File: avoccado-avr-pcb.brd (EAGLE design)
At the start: 17.8 x 40.3 mm, 31 parts, among them IC1 MCP1703CB, Q1 #MHz, Q2 MOSFET-NCHANNEL2N7002PW, U1 ATMEGA168#, U2 MCP73831, X1 Micro USB

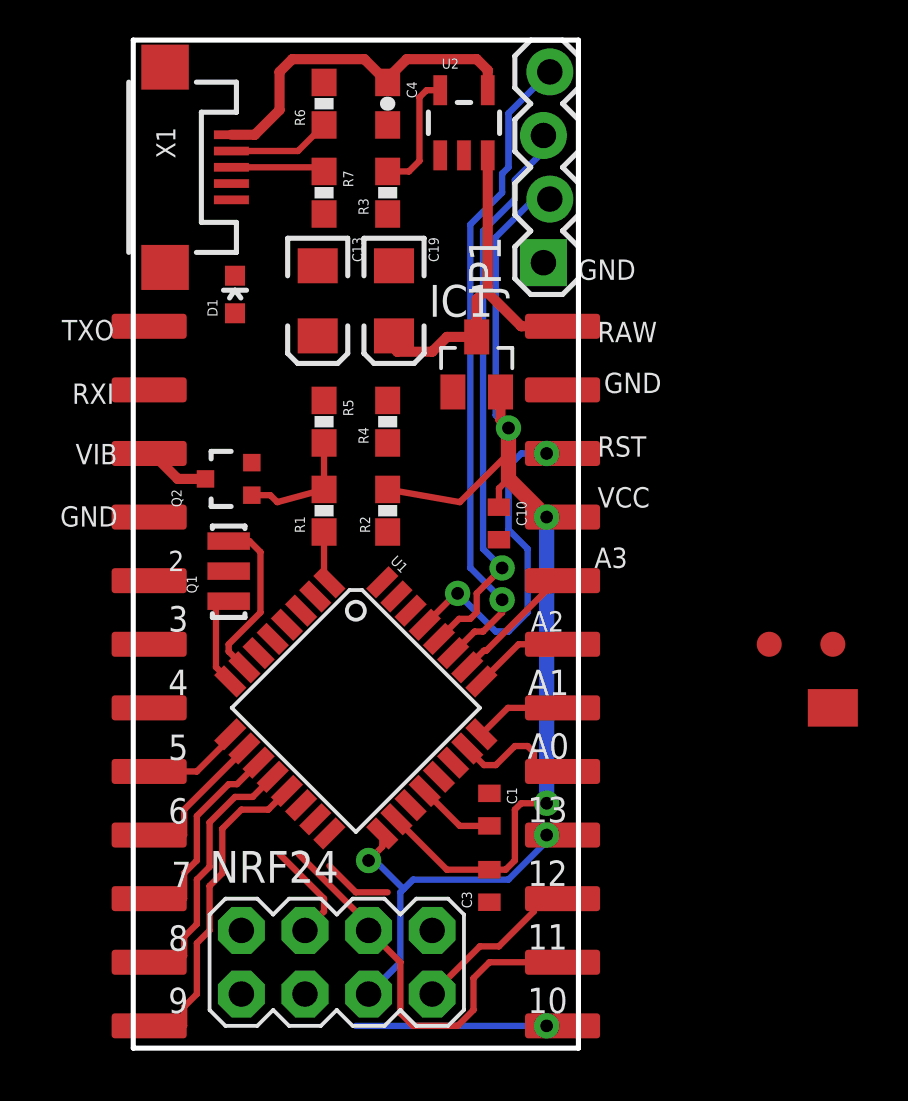
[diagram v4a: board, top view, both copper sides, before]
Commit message: white silkscreen fills at GND pads
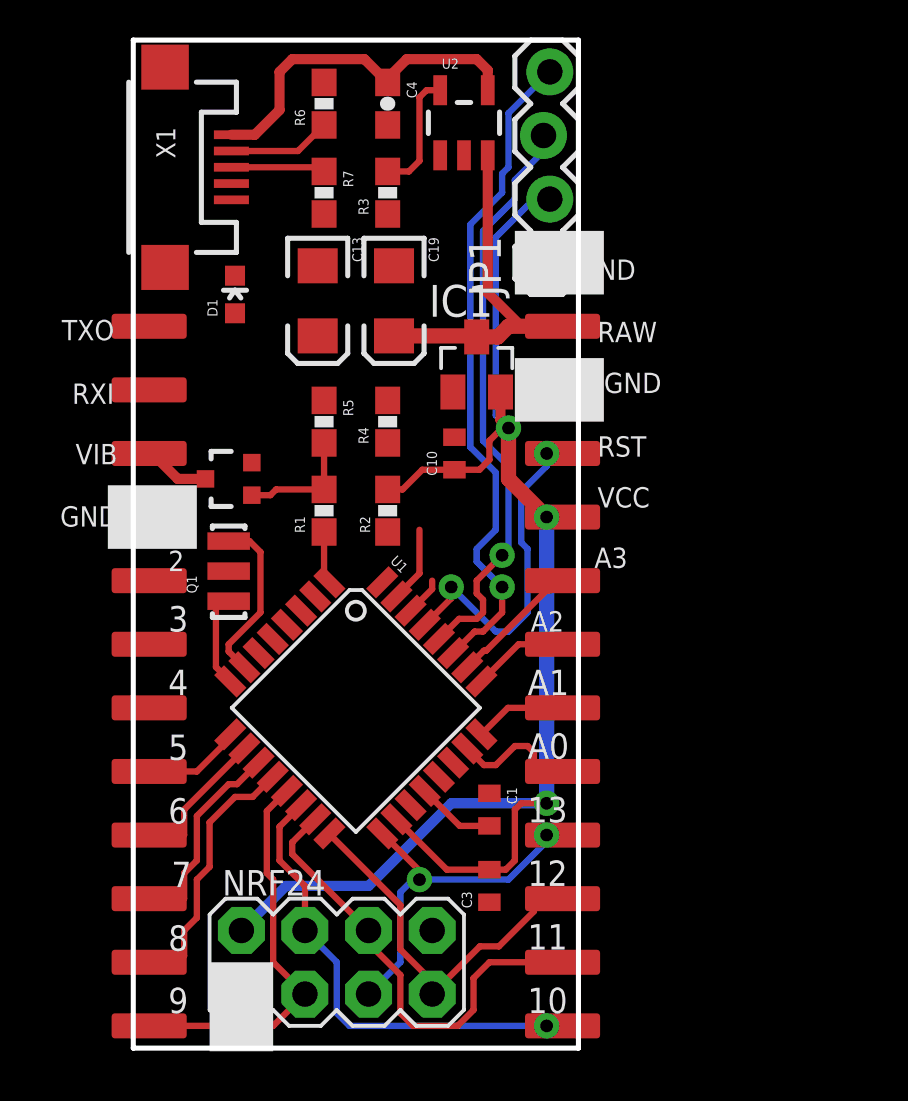
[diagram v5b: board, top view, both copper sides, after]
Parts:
- removed JP4: M01SMD-4.5X1.5, SparkFun-Connectors:PAD-1.5X4.5
- removed U$2, U$4: FIDUCIAL1X2, SparkFun:FIDUCIAL-1X2
- moved C10 3.31 mm to (21.7, 35.6), turned to 90 degrees
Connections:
- removed net 3.3V: NRF24.2
- removed net VCC: C10.1, C13.A, C3.2, IC1.2, JP1.2, JP3.4, R2.2, U1.18, U1.4, U1.6
- new net 3V3: C10.1, C13.A, C3.2, IC1.2, JP1.2, JP3.4, NRF24.2, R2.2, U1.18, U1.4, U1.6
- net D9: now also NRF24.3
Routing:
- net 3V3: track 0.00 -> 59.5 mm, vias 0 -> 3
- net VCC: track 45.8 -> 0.00 mm, vias 3 -> 0
- net D10: track 12.4 -> 18.8 mm
- net MISO: track 9.85 -> 15.2 mm
- net TXO: track 0.00 -> 3.04 mm
- net D9: track 13.1 -> 15.8 mm
- net MOSI: track 16.6 -> 18.4 mm
- net RXI: track 0.00 -> 1.55 mm
- net BAT: track 15.2 -> 16.0 mm
- net SCK: track 15.3 -> 14.6 mm
- net A4: track 26.1 -> 26.7 mm
- net A5: track 22.7 -> 23.3 mm
- net RESET: track 14.1 -> 13.6 mm
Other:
- board text removed: "A4"
- board text removed: "A5"

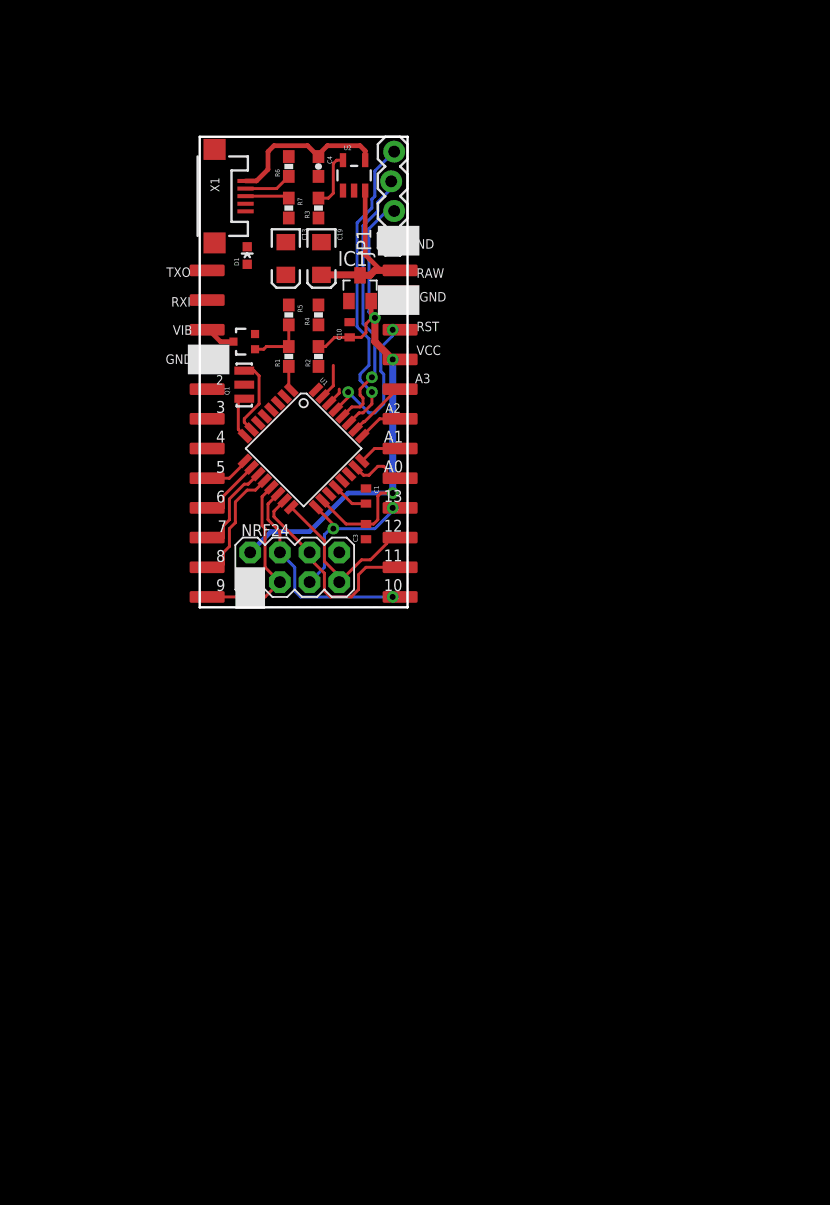
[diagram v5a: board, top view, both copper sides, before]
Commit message: add QFN package for MCU wip
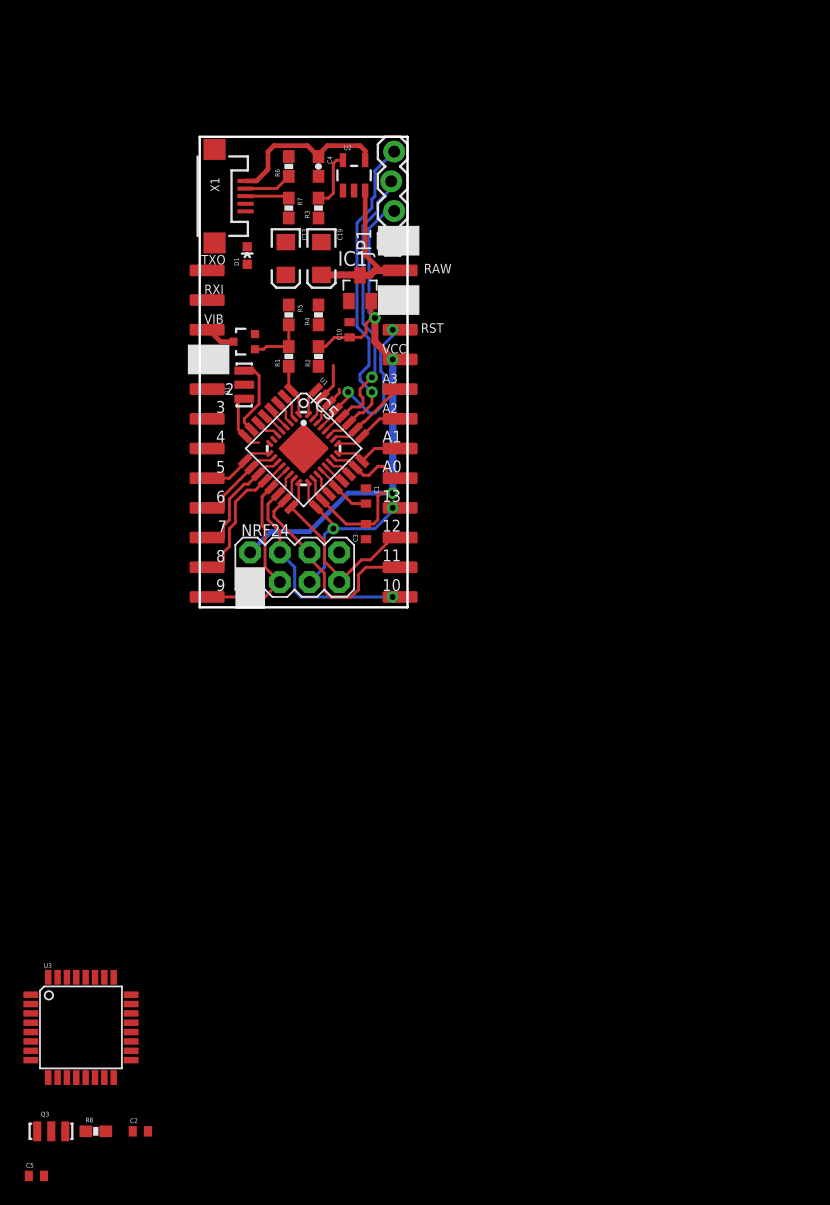
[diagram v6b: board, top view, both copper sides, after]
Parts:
- added C2, C5: 0.1uF, SparkFun:C0402
- added IC5: ATMEGA328P-20MU, idii:MLF32
- added Q3: #MHz, SparkFun:RESONATOR-SMD
- added R8: 10K, SparkFun-Resistors:0603-RES
- added U3: ATMEGA328P, SparkFun-DigitalIC:TQFP32-08
- U1: value ATMEGA168# -> ATMEGA328P; device SparkFun:TQFP32-08 -> SparkFun-DigitalIC:TQFP32-08
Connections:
- new net A6: IC5.19, U1.19, U3.19
- new net A7: IC5.22, U1.22, U3.22
- new net N$10: IC5.8, Q3.3, U3.7
- new net N$9: IC5.7, Q3.1, U3.8
- net 3V3: now also C2.2, IC5.18, IC5.4, IC5.6, R8.2, U3.18, U3.4, U3.6
- net A0: now also IC5.23, U3.23
- net A1: now also IC5.24, U3.24
- net A2: now also IC5.25, U3.25
- net A3: now also IC5.26, U3.26
- net A4: now also IC5.27, U3.27
- net A5: now also IC5.28, U3.28
- net AREF: now also C5.2, IC5.20, U3.20
- net D10: now also IC5.14, U3.14
- net D2: now also IC5.32, U3.32
- net D3: now also IC5.1, U3.1
- net D4: now also IC5.2, U3.2
- net D5: now also IC5.9, U3.9
- net D6: now also IC5.10, U3.10
- net D7: now also IC5.11, U3.11
- net D8: now also IC5.12, U3.12
- net D9: now also IC5.13, U3.13
- net GND: now also C2.1, C5.1, IC5.21, IC5.3, IC5.5, Q3.2, U3.21, U3.3, U3.5
- net MISO: now also IC5.16, U3.16
- net MOSI: now also IC5.15, U3.15
- net RESET: now also IC5.29, R8.1, U3.29
- net RXI: now also IC5.30, U3.30
- net SCK: now also IC5.17, U3.17
- net TXO: now also IC5.31, U3.31
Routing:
- net 3V3: track 59.5 -> 65.9 mm
- net GND: track 0.00 -> 6.14 mm
- net MISO: track 15.2 -> 17.6 mm
- net SCK: track 14.6 -> 17.0 mm
- net D3: track 2.10 -> 4.48 mm
- net D2: track 0.00 -> 2.38 mm
- net A2: track 3.85 -> 6.23 mm
- net D5: track 3.94 -> 6.32 mm
- net A1: track 3.68 -> 6.05 mm
- net D4: track 0.00 -> 2.25 mm
- net A0: track 5.26 -> 7.52 mm
- net A3: track 5.22 -> 7.47 mm
- net D6: track 6.59 -> 8.85 mm
- net MOSI: track 18.4 -> 20.7 mm
- net TXO: track 3.04 -> 5.29 mm
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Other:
- board text removed: "GND"

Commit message: moved Xtal to make room for vias
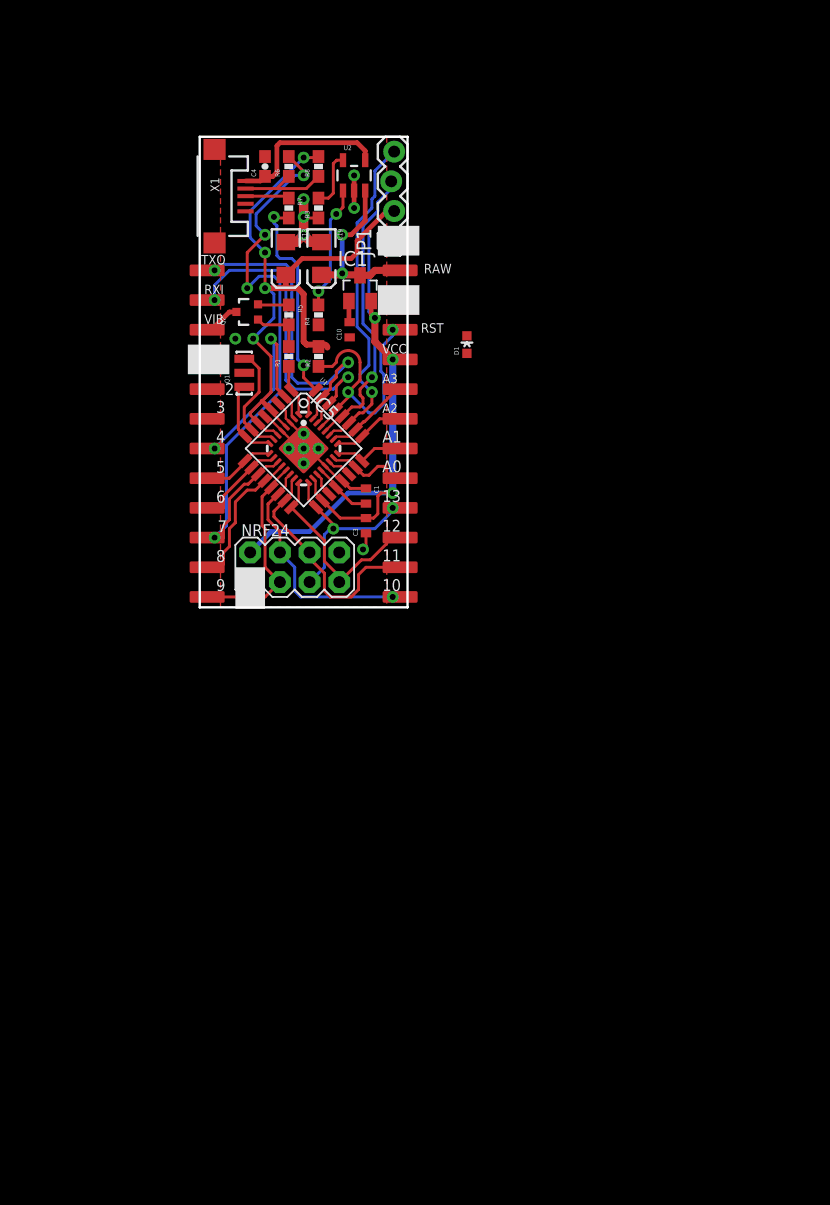
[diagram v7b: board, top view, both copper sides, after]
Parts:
- removed C2, C5: 0.1uF, SparkFun:C0402
- removed Q3: #MHz, SparkFun:RESONATOR-SMD
- removed U3: ATMEGA328P, SparkFun-DigitalIC:TQFP32-08
- R8: value 10K -> 2K
- moved R8 84.7 mm to (19.1, 49.5), turned to 90 degrees
- moved D1 20.3 mm to (31.8, 34.3)
- moved C4 4.57 mm to (14.5, 49.5), turned to 90 degrees
- moved Q2 2.55 mm to (13.0, 37.1)
- moved Q1 1.02 mm to (12.7, 31.9)
- moved C3 0.51 mm to (23.1, 18.8)
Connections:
- net N$7 renamed USB-D+
- removed net N$10: IC5.8, Q3.3, U3.7
- removed net N$8: R6.1, X1.D-
- new net USB-D-: R6.1, R8.1, X1.D-
- net 3V3: no longer C2.2, U3.18, U3.4, U3.6
- net A0: no longer U3.23
- net A1: no longer U3.24
- net A2: no longer U3.25
- net A3: no longer U3.26
- net A4: no longer U3.27
- net A5: no longer U3.28
- net A6: no longer U3.19
- net A7: no longer U3.22
- net AREF: no longer C5.2, U3.20
- net D10: no longer U3.14
- net D2: no longer U3.32
- net D3: no longer U3.1
- net D4: no longer U3.2
- net D5: no longer U3.9
- net D6: no longer U3.10
- net D7: no longer U3.11
- net D8: no longer U3.12
- net D9: no longer U3.13
- net GND: no longer C2.1, C5.1, Q3.2, U3.21, U3.3, U3.5
- net MISO: no longer U3.16
- net MOSI: no longer U3.15
- net N$1: now also IC5.8
- net N$2: now also IC5.7
- net N$9: now also IC5.31; no longer IC5.7, Q3.1, U3.8
- net RESET: no longer R8.1, U3.29
- net RXI: no longer U3.30
- net SCK: no longer U3.17
- net TXO: no longer IC5.31, U3.31
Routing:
- net 3V3: track 65.9 -> 112.7 mm, vias 3 -> 7
- net D7: track 10.4 -> 52.8 mm, vias 0 -> 4
- net GND: track 6.14 -> 33.0 mm, vias 0 -> 14
- net RXI: track 3.66 -> 29.3 mm, vias 0 -> 2
- net TXO: track 5.29 -> 28.8 mm, vias 0 -> 2
- net D2: track 2.38 -> 20.6 mm, vias 0 -> 2
- net D4: track 2.25 -> 19.9 mm, vias 0 -> 2
- net N$4: track 0.00 -> 10.7 mm, vias 0 -> 2
- net USB-D-: track 0.00 -> 8.14 mm
- net RESET: track 15.6 -> 23.1 mm
- net N$8: track 4.13 -> 0.00 mm
- net N$2: track 6.84 -> 9.89 mm
- net N$1: track 5.32 -> 7.23 mm
- net BAT: track 16.0 -> 16.9 mm, vias 0 -> 2
- net VIBR: track 2.67 -> 3.26 mm

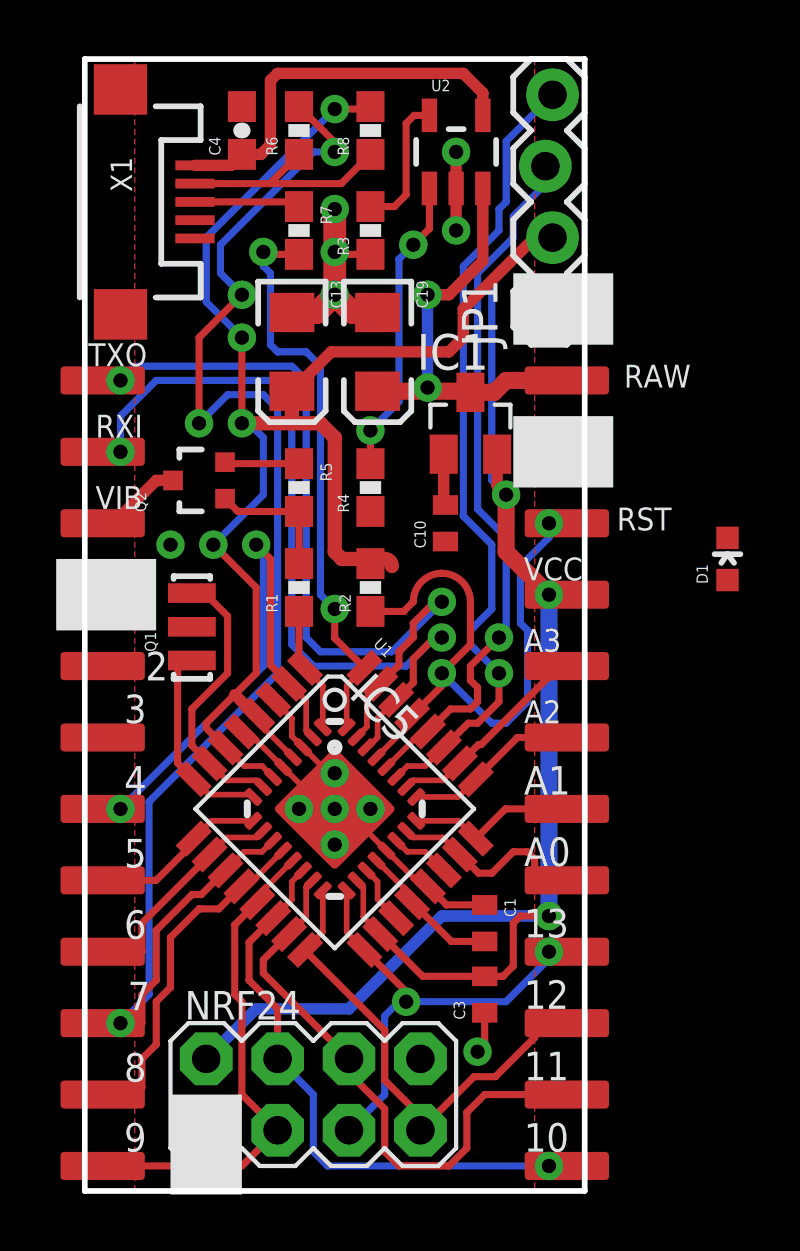
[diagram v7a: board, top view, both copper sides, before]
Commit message: charge indicator wired to MCU
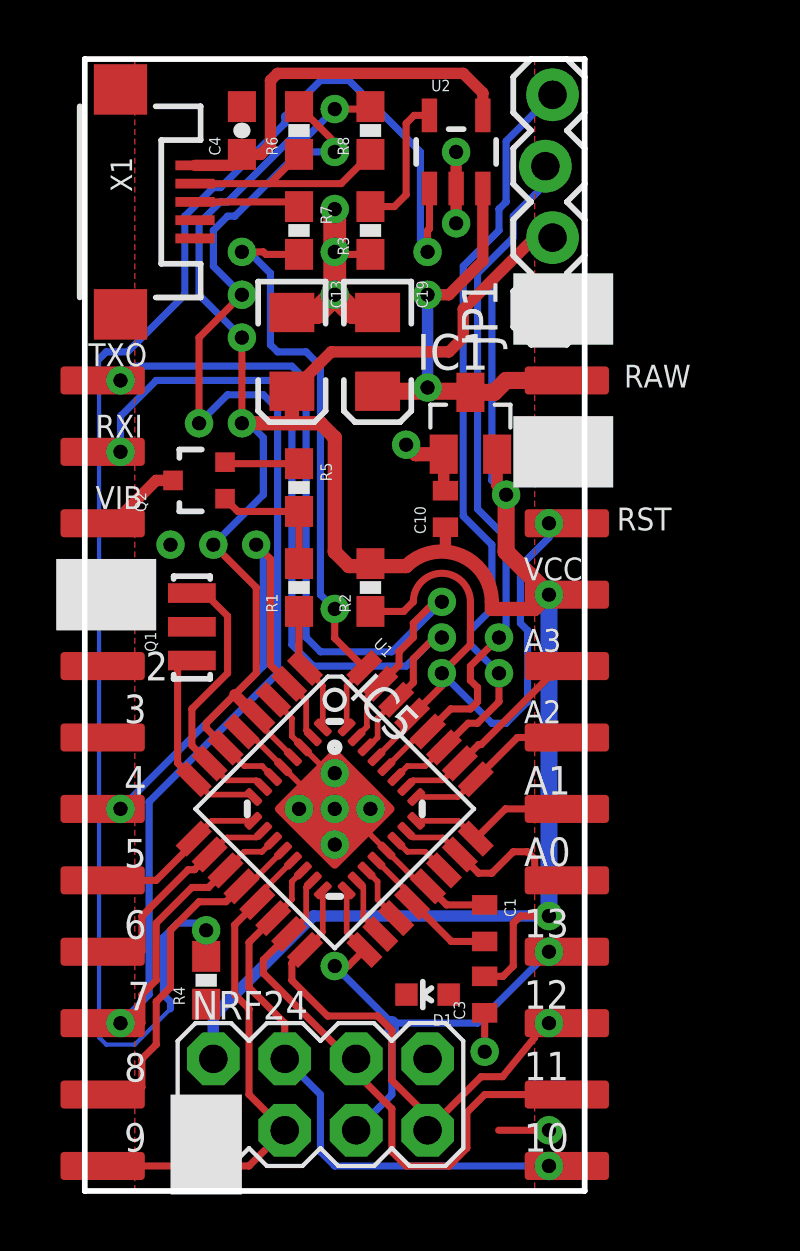
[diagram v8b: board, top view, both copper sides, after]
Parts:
- moved D1 18.8 mm to (21.1, 18.8), turned to 90 degrees
- moved R4 18.5 mm to (13.2, 19.3)
- moved C10 0.51 mm to (21.7, 36.1)
- moved NRF24 0.25 mm to (17.3, 15.2)
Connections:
- removed net N$5: D1.C, R4.1
- net A6: now also D1.C, R4.1
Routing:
- net N$4: track 10.7 -> 57.0 mm
- net 3V3: track 112.7 -> 117.0 mm
- net GND: track 33.0 -> 35.4 mm, vias 14 -> 16
- net MISO: track 17.6 -> 19.0 mm, vias 0 -> 1
- net D2: track 20.6 -> 21.8 mm
- net SCK: track 17.0 -> 18.2 mm
- net RESET: track 23.1 -> 22.2 mm
- net D7: track 52.8 -> 53.6 mm
